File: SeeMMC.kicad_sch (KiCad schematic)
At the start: 17 parts, among them J1 SD_Card, U1 TXS02612RTWR, U2 TPS7A1118PDRV

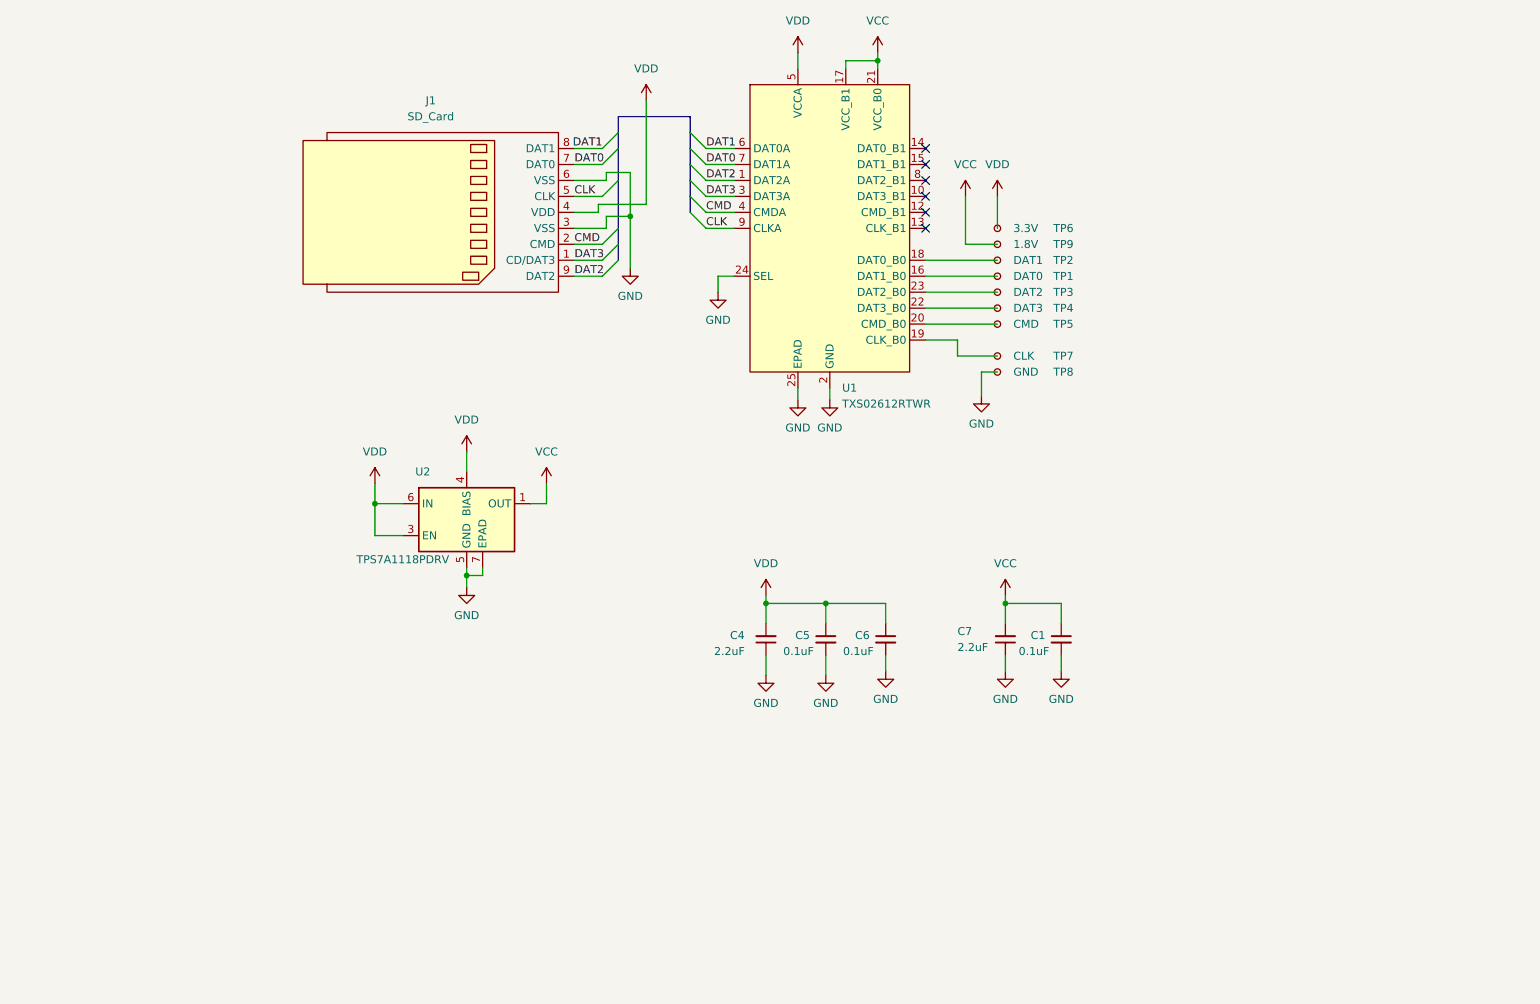
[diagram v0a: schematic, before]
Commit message: Updated KiCad version
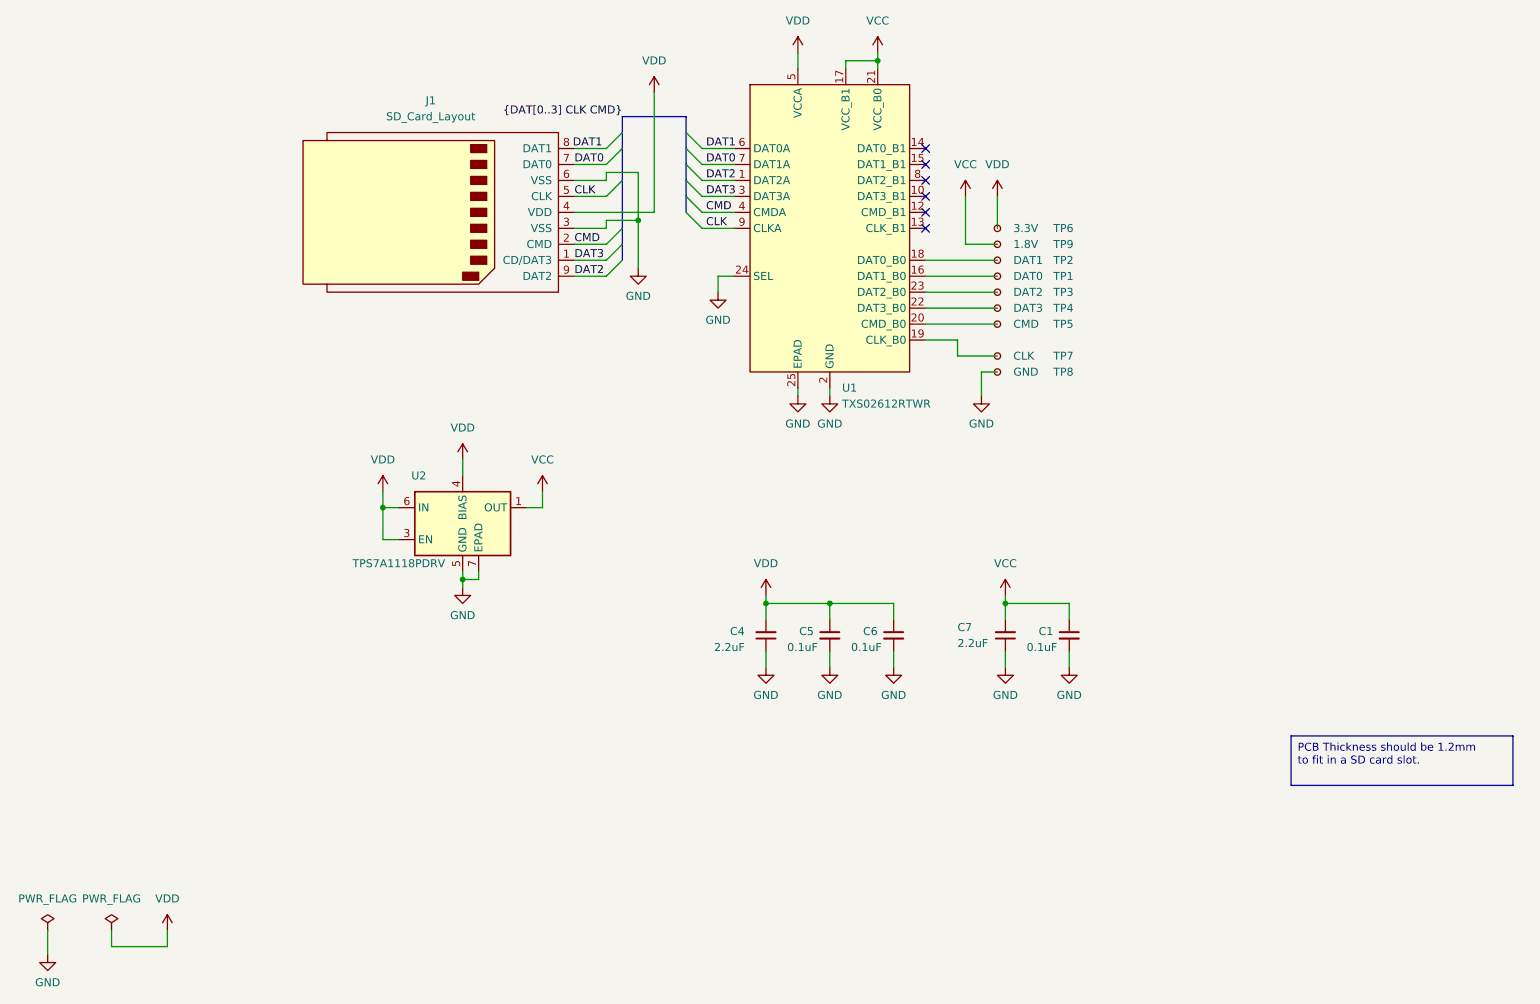
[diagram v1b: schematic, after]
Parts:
- removed J1: SD_Card, Connector_Card:SD_Card_Layout, symbol Connector:SD_Card
- added J1: SD_Card_Layout, Connector_Card:SD_Card_Layout, symbol Connector:SD_Card_Layout
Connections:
- net CLK: now also J1.5 (CLK)
- net CMD: now also J1.2 (CMD)
- net DAT0: now also J1.7 (DAT0)
- net DAT1: now also J1.8 (DAT1)
- net DAT2: now also J1.9 (DAT2)
- net DAT3: now also J1.1 (CD/DAT3)
- net GND: now also J1.3 (VSS), J1.6 (VSS)
- net VDD: now also J1.4 (VDD)
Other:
- moved on the sheet: C1, C4, C5, C6, C7, U2
